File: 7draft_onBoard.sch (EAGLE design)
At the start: 81 parts, among them IC3 74ABT125PW, IC4 MAX4466KS, J2 USB_MINI-B_DIGIKEY, Q1 NPN 40V 1A SOT-23

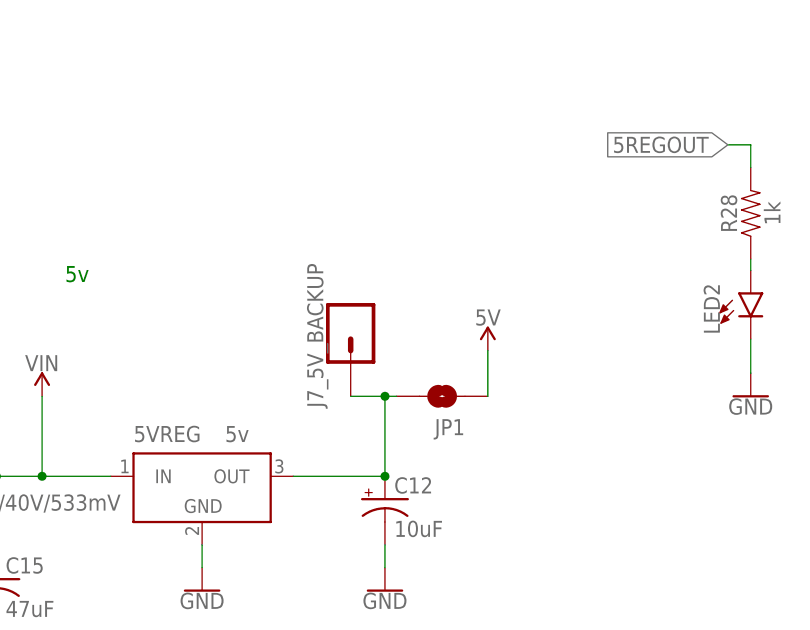
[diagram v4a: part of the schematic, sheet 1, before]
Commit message: everything is added. IR fixed, beam break fixed. neo pixel added for fun this will be addressed at 1 and the one at top is addressed at 2
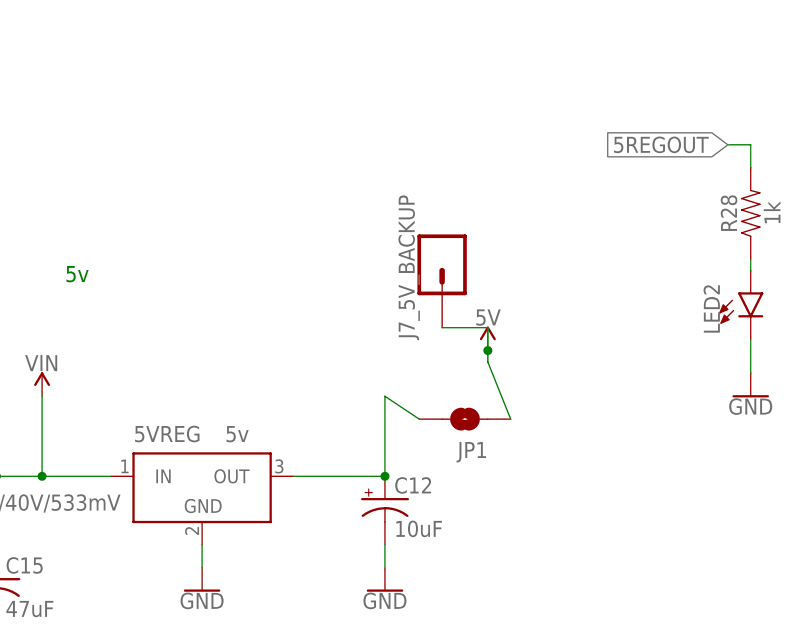
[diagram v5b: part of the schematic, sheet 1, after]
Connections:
- net 5REGOUT: no longer J7_5V_BACKUP.1
- net 5V: now also J7_5V_BACKUP.1
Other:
- moved on the sheet: J7_5V_BACKUP, JP1
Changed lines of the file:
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@@
 <instance part="V_IN" gate="G$1" x="-510.54" y="78.74" rot="MR180"/>
 <instance part="SUPPLY14" gate="G$1" x="-486.41" y="87.63"/>
-<instance part="JP1" gate="G$1" x="-441.96" y="87.63" smashed="yes" rot="R180">
-<attribute name="NAME" x="-439.42" y="85.09" size="1.778" layer="95" font="vector" rot="R180"/>
+<instance part="JP1" gate="G$1" x="-439.42" y="85.09" smashed="yes" rot="R180">
+<attribute name="NAME" x="-436.88" y="82.55" size="1.778" layer="95" font="vector" rot="R180"/>
 </instance>
-<instance part="J7_5V_BACKUP" gate="G$1" x="-452.12" y="95.25" smashed="yes" rot="R270">
-<attribute name="VALUE" x="-456.946" y="97.79" size="1.778" layer="96" font="vector" rot="R270"/>
-<attribute name="NAME" x="-455.168" y="86.36" size="1.778" layer="95" font="vector" rot="R90"/>
+<instance part="J7_5V_BACKUP" gate="G$1" x="-441.96" y="102.87" smashed="yes" rot="R270">
+<attribute name="VALUE" x="-446.786" y="105.41" size="1.778" layer="96" font="vector" rot="R270"/>
+<attribute name="NAME" x="-445.008" y="93.98" size="1.778" layer="95" font="vector" rot="R90"/>
 </instance>
 <instance part="J8_BUZ_B" gate="G$1" x="-439.42" y="8.89" rot="R180"/>
@@
 <pinref part="JP1" gate="G$1" pin="1"/>
 <pinref part="SUPPLY13" gate="G$1" pin="5V"/>
-<wire x1="-436.88" y1="87.63" x2="-436.88" y2="92.71" width="0.1524" layer="91"/>
+<pinref part="J7_5V_BACKUP" gate="G$1" pin="1"/>
+<wire x1="-434.34" y1="85.09" x2="-436.88" y2="91.44" width="0.1524" layer="91"/>
+<wire x1="-441.96" y1="95.25" x2="-436.88" y2="95.25" width="0.1524" layer="91"/>
+<wire x1="-436.88" y1="95.25" x2="-436.88" y2="92.71" width="0.1524" layer="91"/>
+<wire x1="-436.88" y1="92.71" x2="-436.88" y2="91.44" width="0.1524" layer="91"/>
+<junction x="-436.88" y="92.71"/>
 </segment>
 <segment>
@@
 <pinref part="C12" gate="G$1" pin="+"/>
 <wire x1="-458.47" y1="78.74" x2="-448.31" y2="78.74" width="0.1524" layer="91"/>
-<pinref part="J7_5V_BACKUP" gate="G$1" pin="1"/>
-<wire x1="-452.12" y1="87.63" x2="-448.31" y2="87.63" width="0.1524" layer="91"/>
 <wire x1="-448.31" y1="87.63" x2="-448.31" y2="78.74" width="0.1524" layer="91"/>
 <junction x="-448.31" y="78.74"/>
 <pinref part="JP1" gate="G$1" pin="2"/>
-<wire x1="-447.04" y1="87.63" x2="-448.31" y2="87.63" width="0.1524" layer="91"/>
-<junction x="-448.31" y="87.63"/>
-</segment>
-<segment>
+<wire x1="-444.5" y1="85.09" x2="-448.31" y2="87.63" width="0.1524" layer="91"/>
+</segment>
+<segment>
